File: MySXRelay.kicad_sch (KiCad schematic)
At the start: 44 parts, among them J3 Relay, U1 AP2204RA-5.0, U2 BL0942, U3 BP2525X, U4 Si8642BB-B-IS1, U5 MCP1703Ax-180xxTT, U9 ST485E

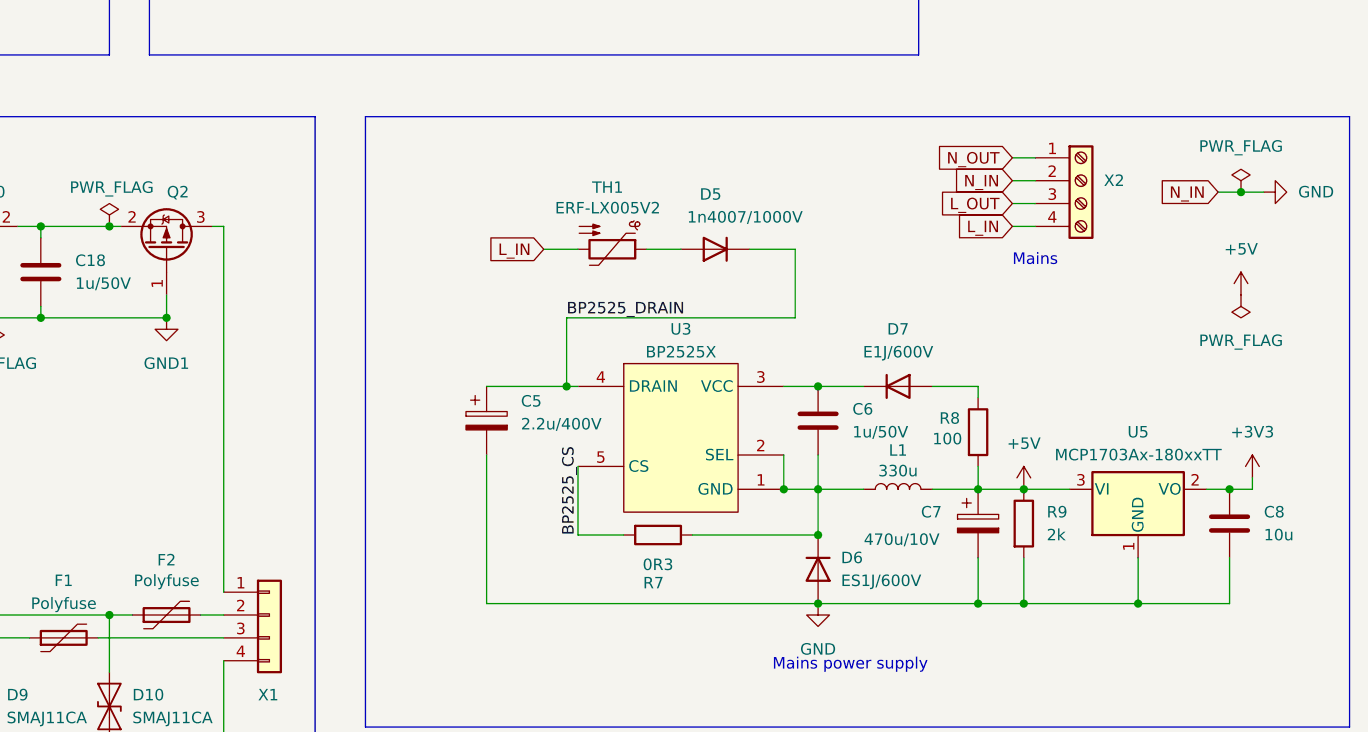
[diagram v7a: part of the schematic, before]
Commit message: add BOM + update schematic parts descriptions
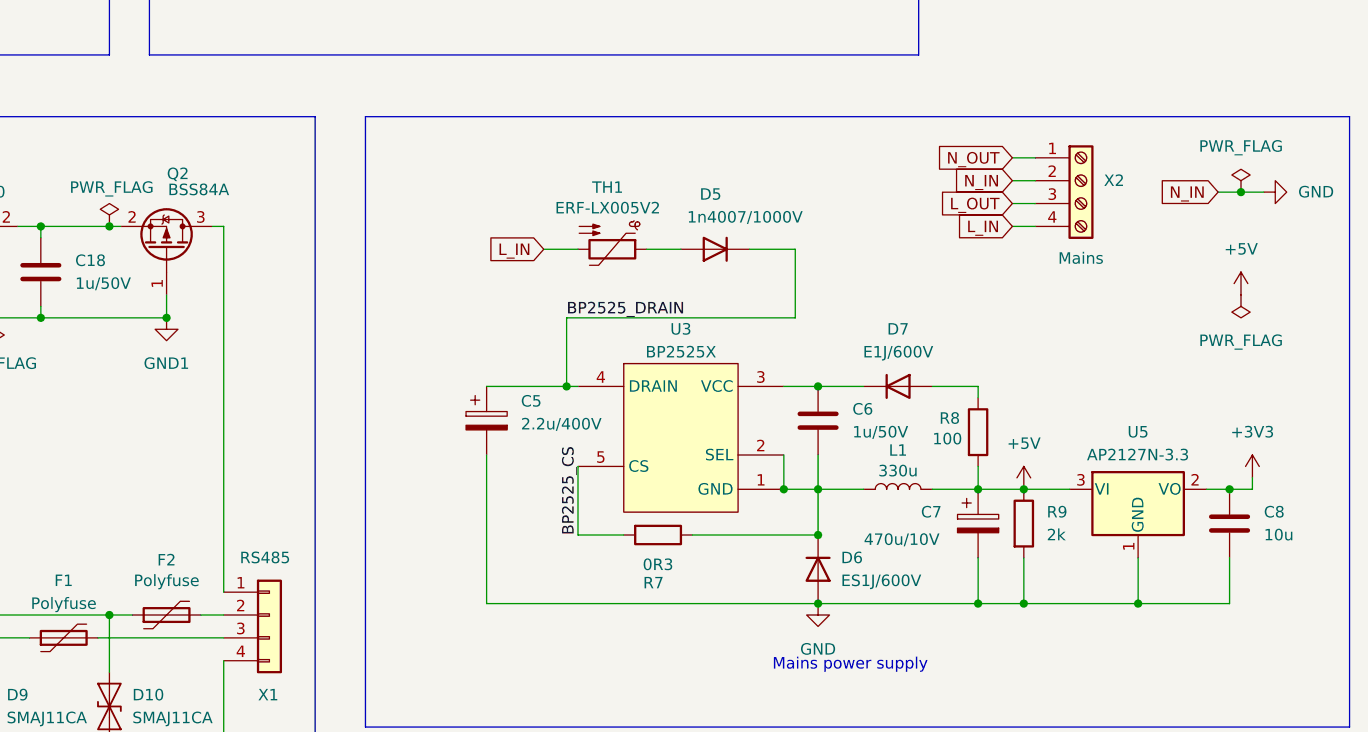
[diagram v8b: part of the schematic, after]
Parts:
- removed U5: MCP1703Ax-180xxTT, Package_TO_SOT_SMD:SOT-23, symbol Regulator_Linear:MCP1703Ax-180xxTT
- added U5: AP2127N-3.3, Package_TO_SOT_SMD:SOT-23, symbol Regulator_Linear:AP2127N-3.3
- Q2: value ~ -> BSS84A
- X1: value ~ -> RS485
- X2: value ~ -> Mains
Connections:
- net +3V3: now also U5.2 (VO)
- net +5V: now also U5.3 (VI)
- net GND: now also U5.1 (GND)
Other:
- note removed: "Mains"
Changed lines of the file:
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@@
 		)
 	)
-	(text "Mains"
-		(exclude_from_sim no)
-		(at 223.52 113.792 0)
-		(effects
-			(font
-				(size 1.27 1.27)
-			)
-			(justify left bottom)
-		)
-	)
 	(text "Bi-stable Relay"
 		(exclude_from_sim no)
@@
 	)
 	(symbol
+		(lib_id "Regulator_Linear:AP2127N-3.3")
+		(at 237.49 138.43 0)
+		(unit 1)
+		(exclude_from_sim no)
+		(in_bom yes)
+		(on_board yes)
+		(dnp no)
+		(fields_autoplaced yes)
+		(property "Reference" "U5"
+			(at 237.49 132.08 0)
+			(effects
+				(font
+					(size 1.27 1.27)
+				)
+			)
+		)
+		(property "Value" "AP2127N-3.3"
+			(at 237.49 134.62 0)
+			(effects
+				(font
+					(size 1.27 1.27)
+				)
+			)
+		)
+		(property "Footprint" "Package_TO_SOT_SMD:SOT-23"
+			(at 237.49 132.715 0)
+			(effects
+				(font
+					(size 1.27 1.27)
+					(italic yes)
+				)
+				(hide yes)
+			)
+		)
+		(property "Datasheet" "https://www.diodes.com/assets/Datasheets/AP2127.pdf"
+			(at 237.49 138.43 0)
+			(effects
+				(font
+					(size 1.27 1.27)
+				)
+				(hide yes)
+			)
+		)
+		(property "Description" "300mA low dropout linear regulator, shutdown pin, 2.5V-6V input voltage, 3.3V fixed positive output, SOT-23 package"
+			(at 237.49 138.43 0)
+			(effects
+				(font
+					(size 1.27 1.27)
+				)
+				(hide yes)
+			)
+		)
+		(pin "1"
+		)
+		(pin "2"
+		)
+		(pin "3"
+		)
+		(instances
+			(project ""
+				(path "/73ae532b-17b2-4152-9abe-0d6b33529f07"
+					(reference "U5")
+					(unit 1)
+				)
+			)
+		)
+	)
+	(symbol
 		(lib_name "GND_1")
 		(lib_id "power:GND")
@@
 			)
 		)
-		(property "Value" "~"
-			(at 144.145 154.94 0)
+		(property "Value" "RS485"
+			(at 137.668 146.05 0)
 			(effects
 				(font
@@
 	)
 	(symbol
-		(lib_id "Regulator_Linear:MCP1703Ax-180xxTT")
-		(at 237.49 138.43 0)
-		(unit 1)
-		(exclude_from_sim no)
-		(in_bom yes)
-		(on_board yes)
-		(dnp no)
-		(fields_autoplaced yes)
-		(property "Reference" "U5"
-			(at 237.49 132.08 0)
-			(effects
-				(font
-					(size 1.27 1.27)
-				)
-			)
-		)
-		(property "Value" "MCP1703Ax-180xxTT"
-			(at 237.49 134.62 0)
-			(effects
-				(font
-					(size 1.27 1.27)
-				)
-			)
-		)
-		(property "Footprint" "Package_TO_SOT_SMD:SOT-23"
-			(at 237.49 133.35 0)
-			(effects
-				(font
-					(size 1.27 1.27)
-				)
-				(hide yes)
-			)
-		)
-		(property "Datasheet" "http://ww1.microchip.com/downloads/en/DeviceDoc/20005122B.pdf"
-			(at 237.49 139.7 0)
-			(effects
-				(font
-					(size 1.27 1.27)
-				)
-				(hide yes)
-			)
-		)
-		(property "Description" "Low Quiescent Current LDO Regulator, 1.8V, 250mA, Vin<=16V, SOT-23"
-			(at 237.49 138.43 0)
-			(effects
-				(font
-					(size 1.27 1.27)
-				)
-				(hide yes)
-			)
-		)
-		(pin "1"
-		)
-		(pin "3"
-		)
-		(pin "2"
-		)
-		(instances
-			(project "MySXRelay"
-				(path "/73ae532b-17b2-4152-9abe-0d6b33529f07"
-					(reference "U5")
-					(unit 1)
-				)
-			)
-		)
-	)
-	(symbol
 		(lib_id "power:GND1")
 		(at 97.79 170.18 0)
@@
 		(on_board yes)
 		(dnp no)
-		(fields_autoplaced yes)
 		(property "Reference" "X2"
 			(at 233.68 104.1399 0)
@@
 			)
 		)
-		(property "Value" "~"
-			(at 233.68 106.6799 0)
+		(property "Value" "Mains"
+			(at 228.6 112.776 0)
 			(effects
 				(font
@@
 		(dnp no)
 		(property "Reference" "Q2"
-			(at 130.81 105.41 90)
+			(at 130.81 103.378 90)
 			(effects
 				(font
@@
 			)
 		)
-		(property "Value" "~"
-			(at 129.54 104.775 90)
+		(property "Value" "BSS84A"
+			(at 133.096 105.156 90)
 			(effects
 				(font
